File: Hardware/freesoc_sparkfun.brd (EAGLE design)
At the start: 116.8 x 53.3 mm, 94 parts, among them J1 POWER_JACKPTH, U1 CY8C5868AXI-LP035, U2 MIC5219 5V, U3 MIC5219 3.3V, U7 CY8C5868LTI-LP039, Y1 32.768kHz

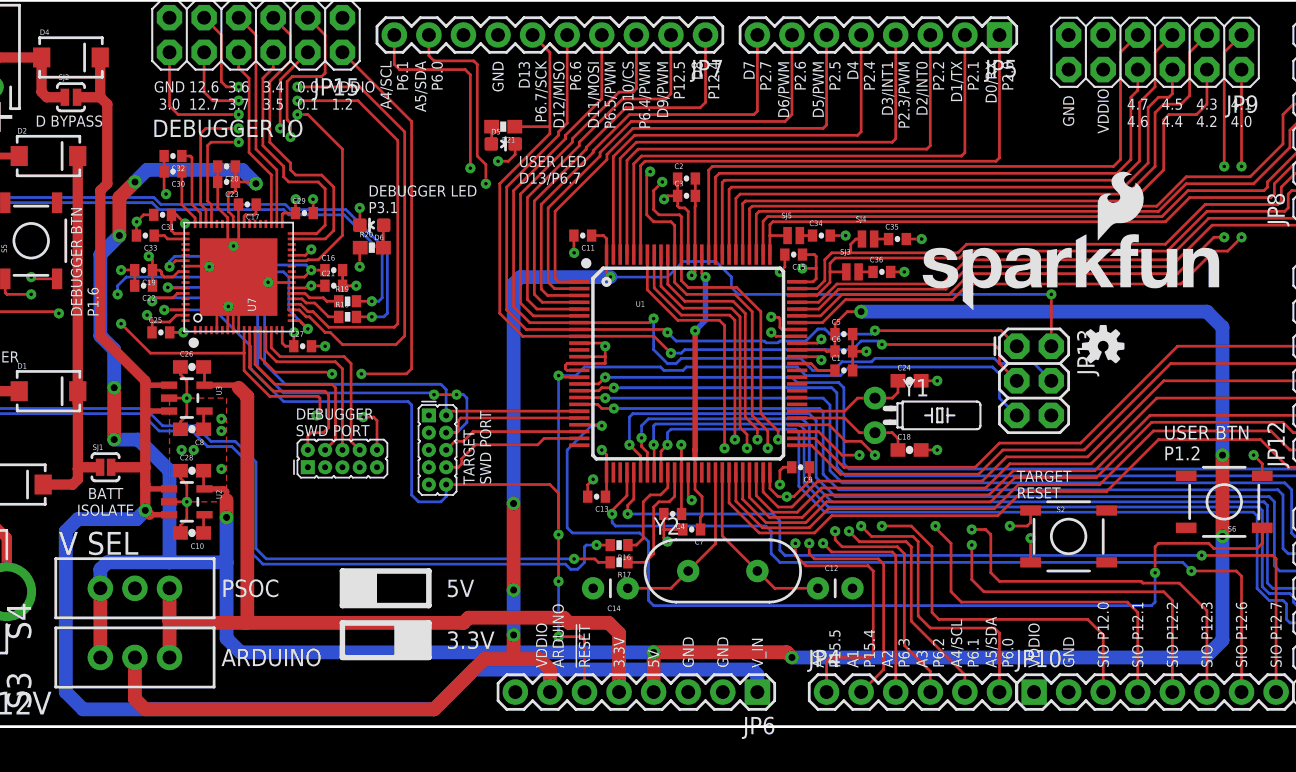
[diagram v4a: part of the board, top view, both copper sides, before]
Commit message: Fixed stuff from QC spreadsheet review.
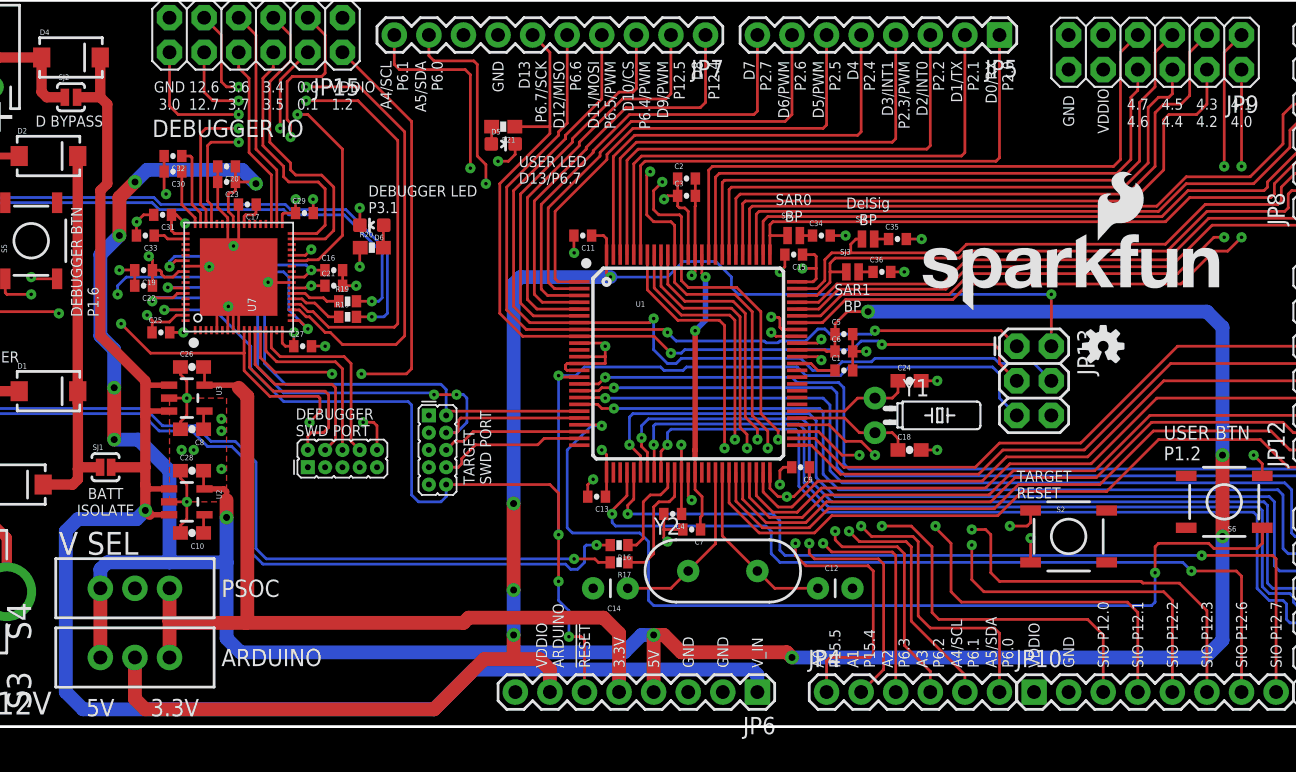
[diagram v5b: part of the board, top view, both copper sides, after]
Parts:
- JP10: value (none) -> 1x8 FEMALE PTH
- JP11, JP12, JP15, JP8, JP9: value 2X6 FEMALE -> 2X6 FEMALE PTH
- JP14, JP17: value M05X20.05_IN_PTH_SILK -> DNP
- JP4: value (none) -> 1X6 FEMALE PTH
- JP5, JP6: value (none) -> 1X8 FEMALE PTH
- JP7: value M10SILK_FEMALE_PTH -> 1X10 FEMALE PTH
- S1, S2, S5, S6: value SWITCH-MOMENTARY-2SMD -> SPST-MOM
- S3, S4: value (none) -> SPDT
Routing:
- net 5V: track 212.3 -> 214.6 mm
- net !DEBUG_RESET: track 39.3 -> 40.1 mm
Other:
- board text added: "DelSig BP"
- board text added: "SAR0 BP"
- board text added: "SAR1 BP"
